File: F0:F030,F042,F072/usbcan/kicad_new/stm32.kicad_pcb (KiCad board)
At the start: 2 copper layers, 64.5 x 26 mm, 54 parts, among them J1 Screw_Terminal_01x03, J10 SDA, J11 PB0, J12 PB1, J13 PB4, J14 PB5, J15 PB2, J16 PB3, J17 GND, J18 GND, J19 +3.3V, J2 SCK, J20 +5V, J21 PA0, J22 PA1, J23 PA2, J24 PA3, J25 PB10, J26 PB11, J3 SWDetc, J4 USB_B, J5 MISO, J6 MOSI, J7 TX, J8 RX, J9 SCL, P1 Hole, P2 Hole, P3 Hole, P4 Hole, Q1 B0505S, SW1 SW_DIP_x01, U1 LM1117-3.3, U2 USBLC6-2SC6, U3 STM32F072C8Tx, U4 ISO1050DUB

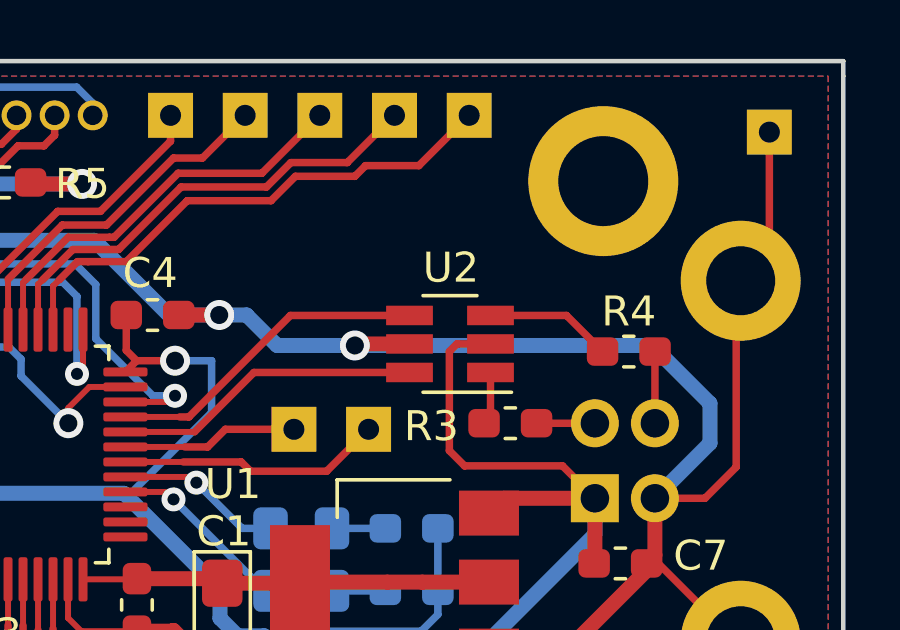
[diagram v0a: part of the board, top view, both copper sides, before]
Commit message: fixed bug with usblc6 on usbcan
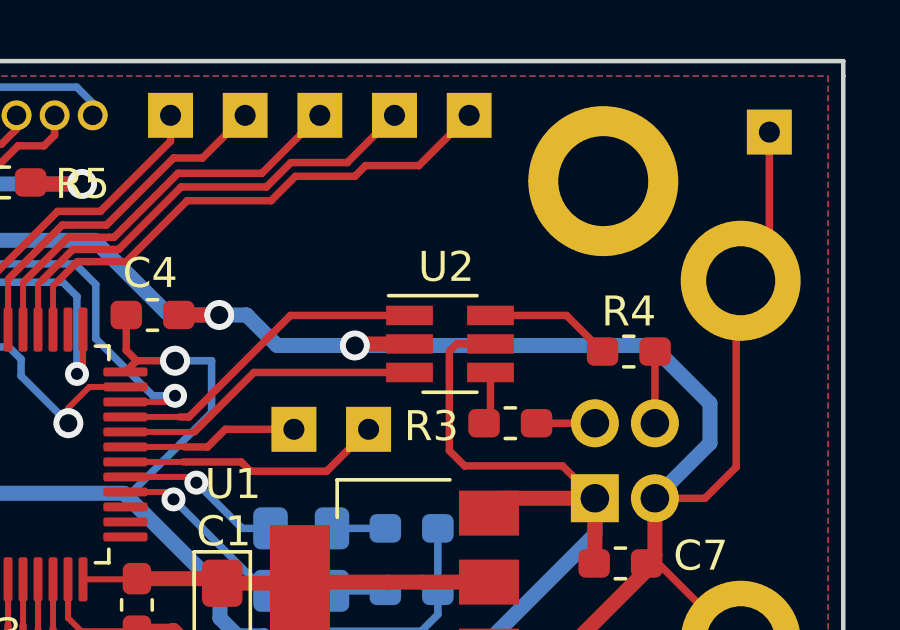
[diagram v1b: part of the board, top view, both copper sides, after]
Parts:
- turned U2 to 0 degrees
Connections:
- U2 pad 1: Net-(R3-Pad2) -> Net-(U2-Pad1)
- U2 pad 2: +5V -> GND
- U2 pad 3: Net-(R4-Pad2) -> Net-(U2-Pad3)
- U2 pad 4: Net-(U3-Pad33) -> Net-(R3-Pad2)
- U2 pad 5: GND -> +5V
- U2 pad 6: Net-(U3-Pad32) -> Net-(R4-Pad2)
- U3 pad 32: Net-(U3-Pad32) -> Net-(U2-Pad3)
- U3 pad 33: Net-(U3-Pad33) -> Net-(U2-Pad1)
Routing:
- net Net-(U3-Pad33): track 10.9 -> 0.00 mm
- net Net-(U2-Pad1): track 0.00 -> 10.9 mm
- net Net-(U3-Pad32): track 10.3 -> 0.00 mm
- net Net-(U2-Pad3): track 0.00 -> 10.3 mm
